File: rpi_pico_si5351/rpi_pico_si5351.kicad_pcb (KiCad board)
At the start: 2 copper layers, 100 x 50 mm, 38 parts, among them J1 CLK0, J2 CLK1, J3 CLK2, SW1 JS5208, SW2 PEC12R-3220F-S0024, U1 ER-TFT020-2, U2 Pico, U3 MS5351M, X1 MCSJK-7U-27.00-10-10-60-B-10

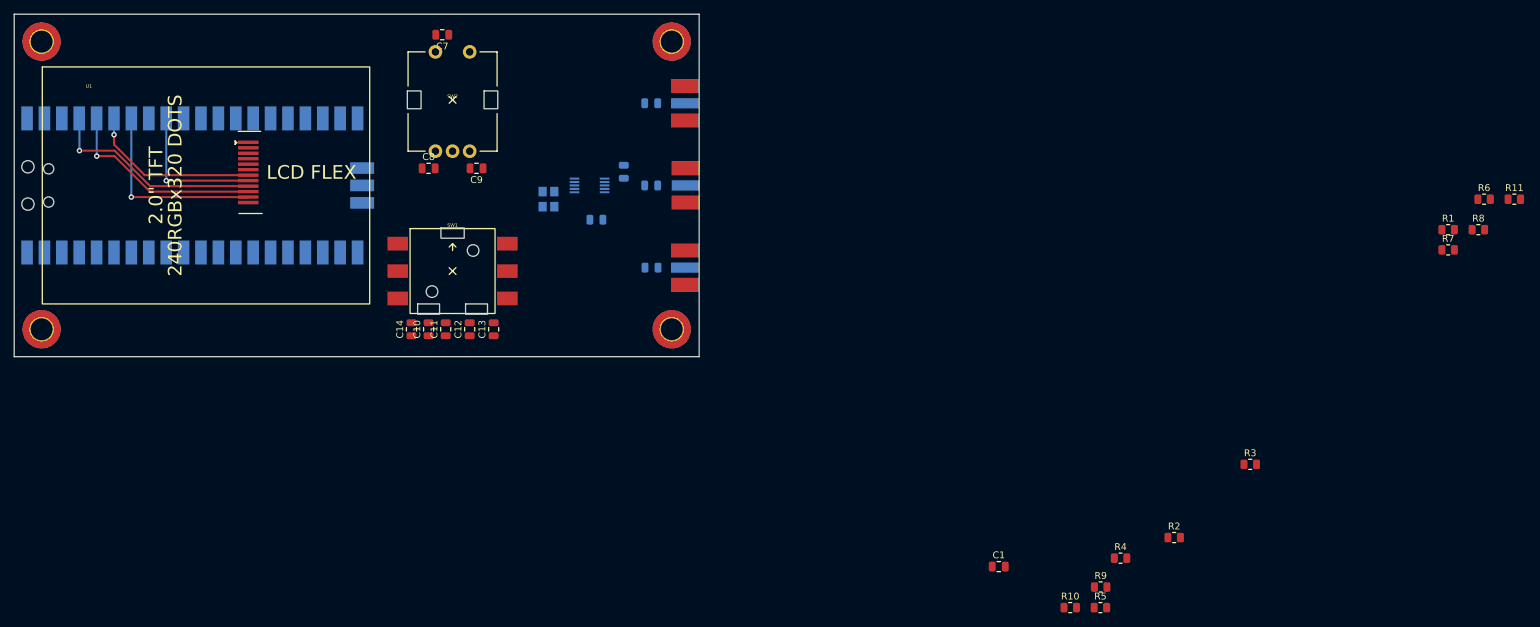
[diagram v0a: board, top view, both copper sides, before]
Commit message: fix footprints, update schematic
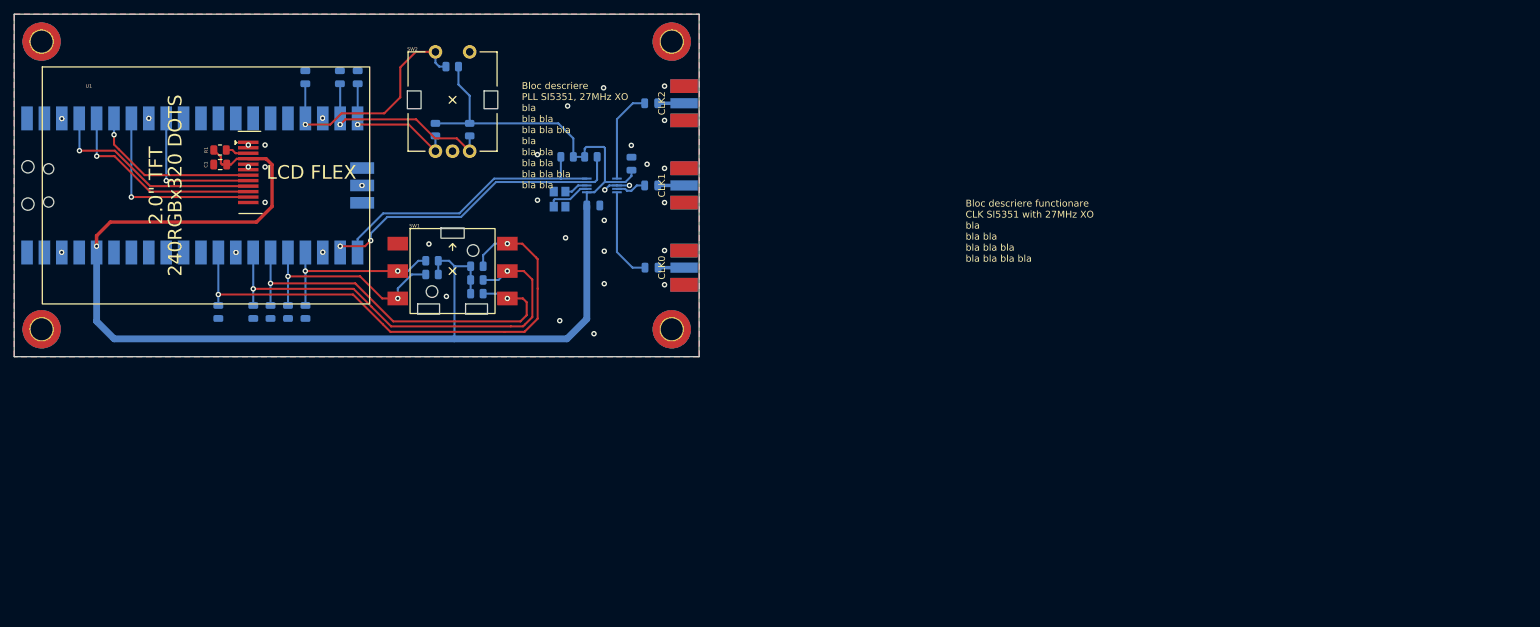
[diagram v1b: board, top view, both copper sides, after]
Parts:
- C10, C11, C12, C13, C14, C7, C8, C9, R10, R11, R2, R3, R4, R5, R6, R7, R8, R9: moved to B.Cu
- moved R1 179.7 mm to (60.0, 44.8), turned to 180 degrees
- moved R8 152.9 mm to (91.0, 63.0), turned to 180 degrees
- moved R11 152.9 mm to (96.5, 41.9), turned to -90 degrees
- moved R6 147.5 mm to (97.5, 63.8)
- moved R7 142.0 mm to (97.5, 65.8)
- moved C1 127.9 mm to (60.1, 47.0), turned to 180 degrees
- moved R9 121.4 mm to (94.0, 32.6), turned to 180 degrees
- moved R10 116.0 mm to (91.5, 41.9), turned to -90 degrees
- moved R4 109.5 mm to (91.0, 61.0), turned to 180 degrees
- moved R3 106.2 mm to (114.2, 45.8), turned to 180 degrees
- moved R2 104.6 mm to (110.7, 45.8)
- moved R5 103.8 mm to (97.5, 61.8)
- moved C11 33.3 mm to (59.8, 68.5)
- moved C13 32.7 mm to (67.4, 68.5)
- moved C12 31.7 mm to (64.9, 68.5)
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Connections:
- net Net-(C2-Pad2) renamed /CLK0
- net Net-(C5-Pad2) renamed /CLK1
- net Net-(C6-Pad2) renamed /CLK2
- U2 pad 17: unconnected-(U2-Pad17) -> ENC_SW
- U2 pad 19: unconnected-(U2-Pad19) -> ENC_B
- U2 pad 20: unconnected-(U2-Pad20) -> ENC_A
- U2 pad 24: unconnected-(U2-Pad24) -> JOY_LEFT
- U2 pad 25: unconnected-(U2-Pad25) -> JOY_PUSH
- U2 pad 26: unconnected-(U2-Pad26) -> JOY_DOWN
- U2 pad 27: unconnected-(U2-Pad27) -> JOY_RIGHT
- U2 pad 29: unconnected-(U2-Pad29) -> JOY_UP
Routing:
- net +3V3: track 0.00 -> 222.6 mm, vias 0 -> 1
- net JOY_UP: track 0.00 -> 78.2 mm, vias 0 -> 2
- net JOY_RIGHT: track 0.00 -> 65.9 mm, vias 0 -> 2
- net JOY_DOWN: track 0.00 -> 57.5 mm, vias 0 -> 2
- net SI5351_SCL: track 0.00 -> 45.5 mm, vias 0 -> 2
- net SI5351_SDA: track 0.00 -> 41.4 mm
- net ENC_SW: track 0.00 -> 35.3 mm, vias 0 -> 1
- net JOY_PUSH: track 0.00 -> 32.5 mm, vias 0 -> 2
- net ENC_B: track 0.00 -> 29.4 mm, vias 0 -> 1
- net JOY_LEFT: track 0.00 -> 26.9 mm, vias 0 -> 2
- net ENC_A: track 0.00 -> 21.2 mm, vias 0 -> 1
- net Net-(C2-Pad1): track 0.00 -> 13.8 mm
- net Net-(C6-Pad1): track 0.00 -> 13.7 mm
- net Net-(U3-Pad2): track 0.00 -> 6.46 mm
- net Net-(C5-Pad1): track 0.00 -> 4.48 mm
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- added copper zone on B.Cu, net GND
- added copper zone on F.Cu, net GND
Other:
- board text added: "Bloc descriere PLL SI5351, 27MHz XO bla bla bla bla bla bla bla bla bla bla bla bla bla bla bla bla"
- board text added: "Bloc descriere functionare CLK SI5351 with 27MHz XO bla bla bla bla bla bla bla bla bla bla"
- board text added: "CLK0"
- board text added: "CLK1"
- board text added: "CLK2"

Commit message: add multi-board header to allow stacking of multiple modules
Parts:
- added J4: SSM-120-F-DV, Connector_PinSocket_2.54mm:PinSocket_2x20_P2.54mm_Vertical_SMD, B.Cu at (64.0, 31.0)
- R2, R3: value 4.7k -> 2.2K
- U2: value Pico -> RP2040-PICO30; footprint MCU_RaspberryPi_and_Boards:RPi_Pico_SMD_TH -> parts:RP2040_PICO30_SMD
- moved C9 23.9 mm to (97.5, 47.4), turned to 180 degrees
- moved C7 20.8 mm to (92.4, 28.1), turned to 180 degrees
- moved C8 16.8 mm to (90.5, 47.4), turned to 0 degrees
- moved R2 4.41 mm to (115.1, 45.3), turned to 90 degrees
- moved R3 3.48 mm to (110.7, 45.8), turned to 0 degrees
- moved U2 0.05 mm to (56.1, 50.0)
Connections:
- net +3V3 renamed 3V3_OUT
- net ENC_A renamed GPIO15
- net ENC_B renamed GPIO14
- net ENC_SW renamed GPIO13
- net JOY_DOWN renamed GPIO20
- net JOY_LEFT renamed GPIO18
- net JOY_PUSH renamed GPIO19
- net JOY_RIGHT renamed GPIO21
- net JOY_UP renamed GPIO22
- net TFT_CS renamed GPIO6
- net TFT_DC renamed GPIO4
- net TFT_RST renamed GPIO5
- net TFT_SCK renamed GPIO2
- net TFT_TX renamed GPIO3
- R2 pad 1: SI5351_SDA -> GPIO17
- R3 pad 1: SI5351_SCL -> GPIO16
- U2 pad 1: unconnected-(U2-Pad1) -> GPIO0
- U2 pad 10: unconnected-(U2-Pad10) -> GPIO7
- U2 pad 11: unconnected-(U2-Pad11) -> GPIO8
- U2 pad 12: unconnected-(U2-Pad12) -> GPIO9
- U2 pad 13: unconnected-(U2-Pad13) -> GPIO29
- U2 pad 14: unconnected-(U2-Pad14) -> GPIO10
- U2 pad 15: unconnected-(U2-Pad15) -> GPIO11
- U2 pad 16: unconnected-(U2-Pad16) -> GPIO12
- U2 pad 18: GND -> GPIO25
- U2 pad 2: unconnected-(U2-Pad2) -> GPIO1
- U2 pad 21: SI5351_SDA -> GPIO16
- U2 pad 22: SI5351_SCL -> GPIO17
- U2 pad 23: GND -> GPIO24
- U2 pad 28: GND -> GPIO23
- U2 pad 30: unconnected-(U2-Pad30) -> RUN
- U2 pad 31: unconnected-(U2-Pad31) -> GPIO26
- U2 pad 32: unconnected-(U2-Pad32) -> GPIO27
- U2 pad 34: unconnected-(U2-Pad34) -> GPIO28
- U2 pad 35: unconnected-(U2-Pad35) -> ADC_VREF
- U2 pad 37: unconnected-(U2-Pad37) -> 3V3_EN
- U2 pad 39: unconnected-(U2-Pad39) -> VDD_SYS
- U2 pad 40: unconnected-(U2-Pad40) -> VBUS
- U3 pad 4: SI5351_SCL -> GPIO17
- U3 pad 5: SI5351_SDA -> GPIO16
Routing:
- net GPIO17: track 0.00 -> 80.0 mm, vias 0 -> 3
- net GPIO16: track 0.00 -> 77.5 mm, vias 0 -> 2
- net SI5351_SCL: track 45.5 -> 0.00 mm, vias 2 -> 0
- net SI5351_SDA: track 41.4 -> 0.00 mm
- net 3V3_EN: track 0.00 -> 37.3 mm, vias 0 -> 2
- net GPIO27: track 0.00 -> 36.3 mm, vias 0 -> 2
- net GPIO28: track 0.00 -> 35.4 mm, vias 0 -> 2
- net VBUS: track 0.00 -> 35.1 mm, vias 0 -> 2
- net GPIO22: track 78.2 -> 113.1 mm, vias 2 -> 4
- net VDD_SYS: track 0.00 -> 34.7 mm, vias 0 -> 2
- net 3V3_OUT: track 222.6 -> 257.2 mm, vias 1 -> 2
- net ADC_VREF: track 0.00 -> 34.6 mm, vias 0 -> 2
- net RUN: track 0.00 -> 34.5 mm, vias 0 -> 2
- net GPIO21: track 65.9 -> 100.4 mm, vias 2 -> 4
- net GPIO24: track 0.00 -> 34.5 mm, vias 0 -> 2
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- added copper zone on In1.Cu, net GND
- added copper zone on In2.Cu, net GND
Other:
- copper layers 2 -> 4
- board text added: "CENTERED AT : X34 Y6 FROM TOP LEFT CORNER"
- board text added: "ENCODER"
- board text added: "JOYSTICK"
- board text added: "RPI CONTROL MODULE 1. Stand-alone signal generator with SI5351 installed 2. System controller multiple boards stacked via the exptansion header"
- board text removed: "Bloc descriere PLL SI5351, 27MHz XO bla bla bla bla bla bla bla bla bla bla bla bla bla bla bla bla"
- board text removed: "Bloc descriere functionare CLK SI5351 with 27MHz XO bla bla bla bla bla bla bla bla bla bla"
